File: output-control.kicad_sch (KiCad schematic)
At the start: 57 parts, among them U16 ADS7828, U17 TCA9534PWR, U18 ADS7828

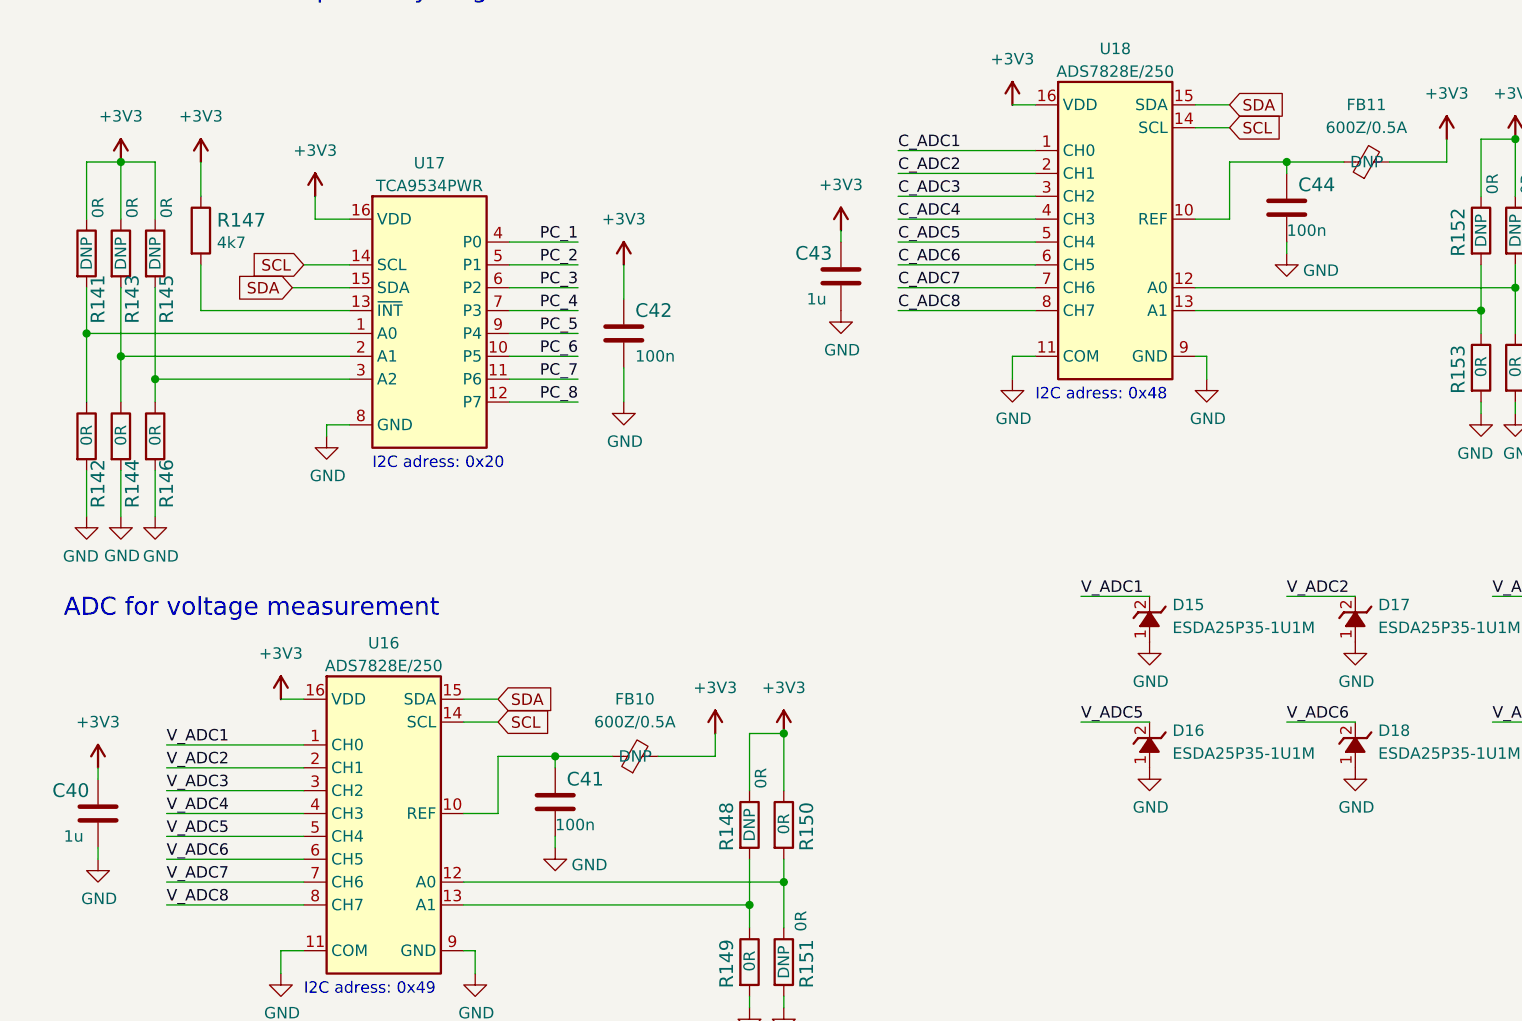
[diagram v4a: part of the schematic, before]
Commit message: Standarize mechanicals and output control
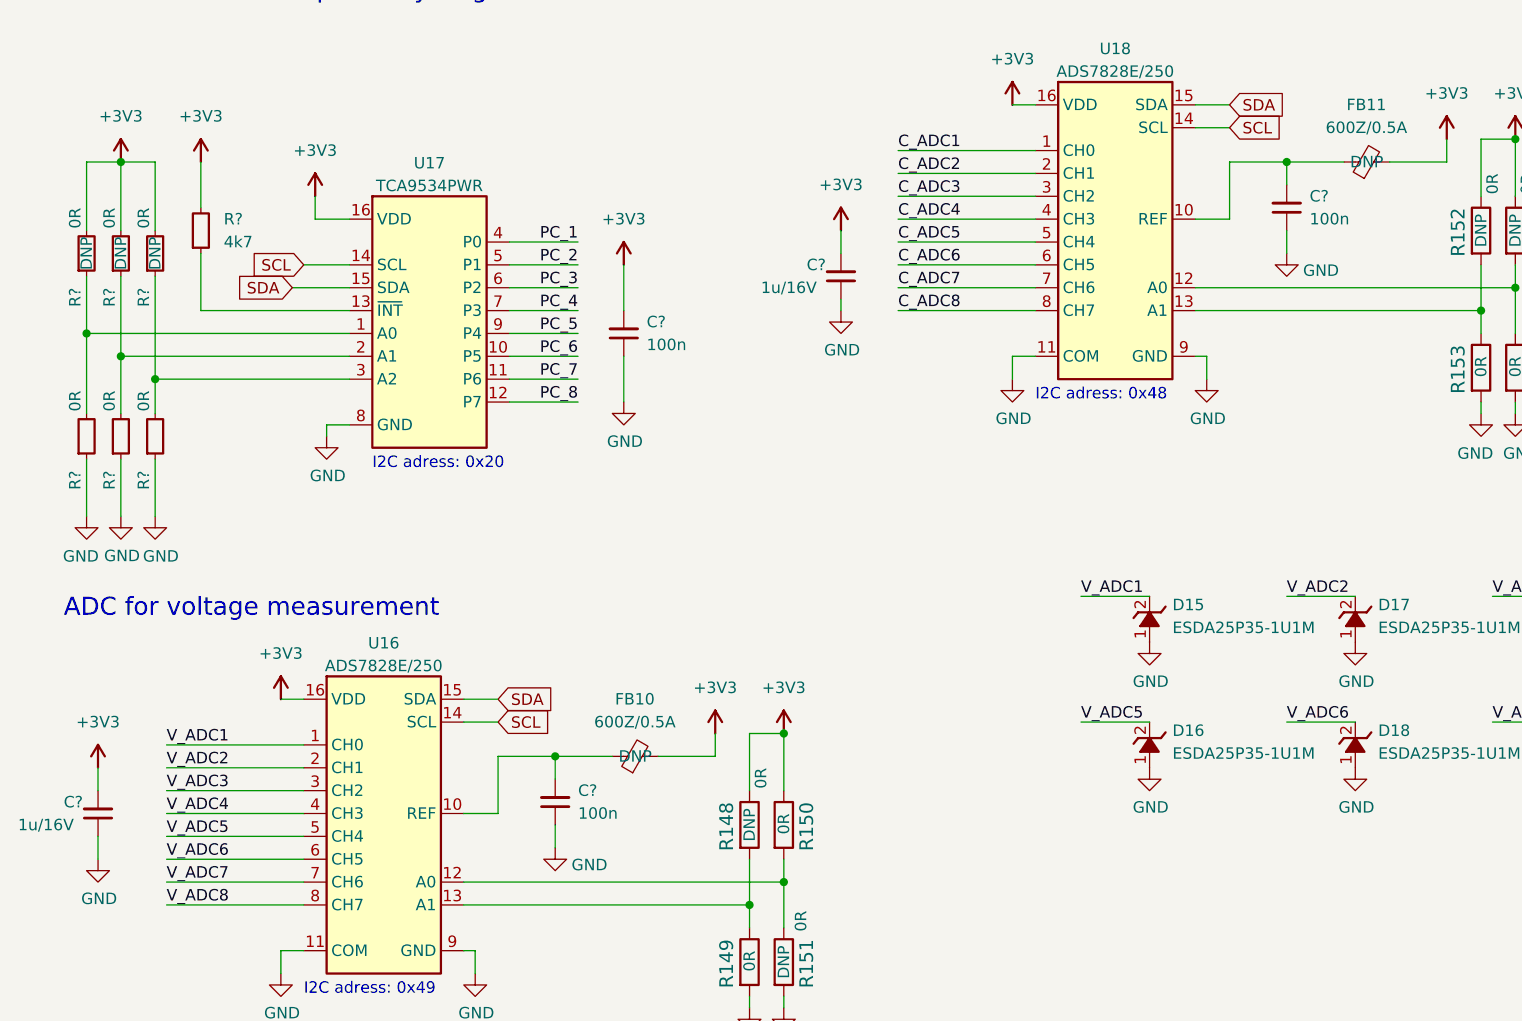
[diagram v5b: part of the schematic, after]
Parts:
- removed C40, C43: C_1u_0402, antmicro-footprints:C_0402_1005Metric, symbol antmicroCapacitors0402:C_1u_0402
- removed C41, C42, C44: C_100n_0402, antmicro-footprints:C_0402_1005Metric, symbol antmicroCapacitors0402:C_100n_0402
- removed R141, R142, R143, R144, R145, R146: R_0R_0402, antmicro-footprints:R_0402_1005Metric, symbol antmicroResistors0402:R_0R_0402
- removed R147: R_4k7_0402, antmicro-footprints:R_0402_1005Metric, symbol antmicroResistors0402:R_4k7_0402
- added C? (x3): C_100n_0402, antmicro-footprints:C_0402_1005Metric, symbol antmicroCapacitors0402:C_100n_0402
- added C? (x2): C_1u_16V_0402, antmicro-footprints:C_0402_1005Metric, symbol antmicroCapacitors0402:C_1u_16V_0402
- added R? (x6): R_0R_0402, antmicro-footprints:R_0402_1005Metric, symbol antmicroResistors0402:R_0R_0402
- added R?: R_4k7_0402, antmicro-footprints:R_0402_1005Metric, symbol antmicroResistors0402:R_4k7_0402
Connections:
- net +3V3: now also C?.2, C?.2, C?.2, R?.2, R?.2, R?.2, R?.2
- net GND: now also C?.1, C?.1, C?.1, C?.1, C?.1, R?.1, R?.1, R?.1
- net at U17.1 (A0): now also R?.1, R?.2
- net at U17.13 (~{INT}): now also R?.1
- net at FB11.1, U18.10 (REF): now also C?.2
- net at U17.2 (A1): now also R?.1, R?.2
- net at FB10.1, U16.10 (REF): now also C?.2
- net at U17.3 (A2): now also R?.1, R?.2

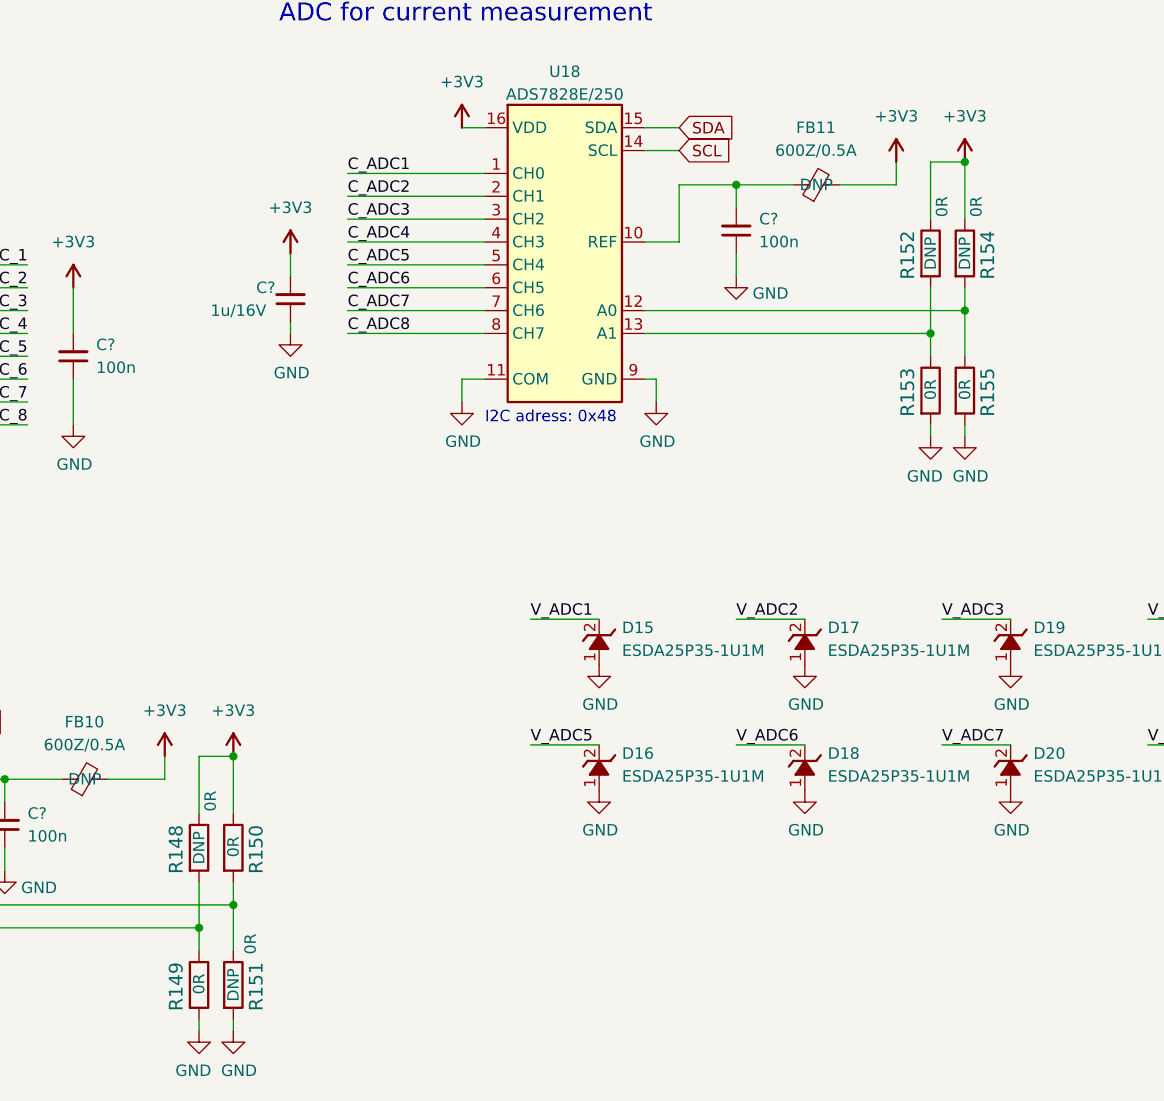
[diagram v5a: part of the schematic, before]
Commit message: Replace outpouts components
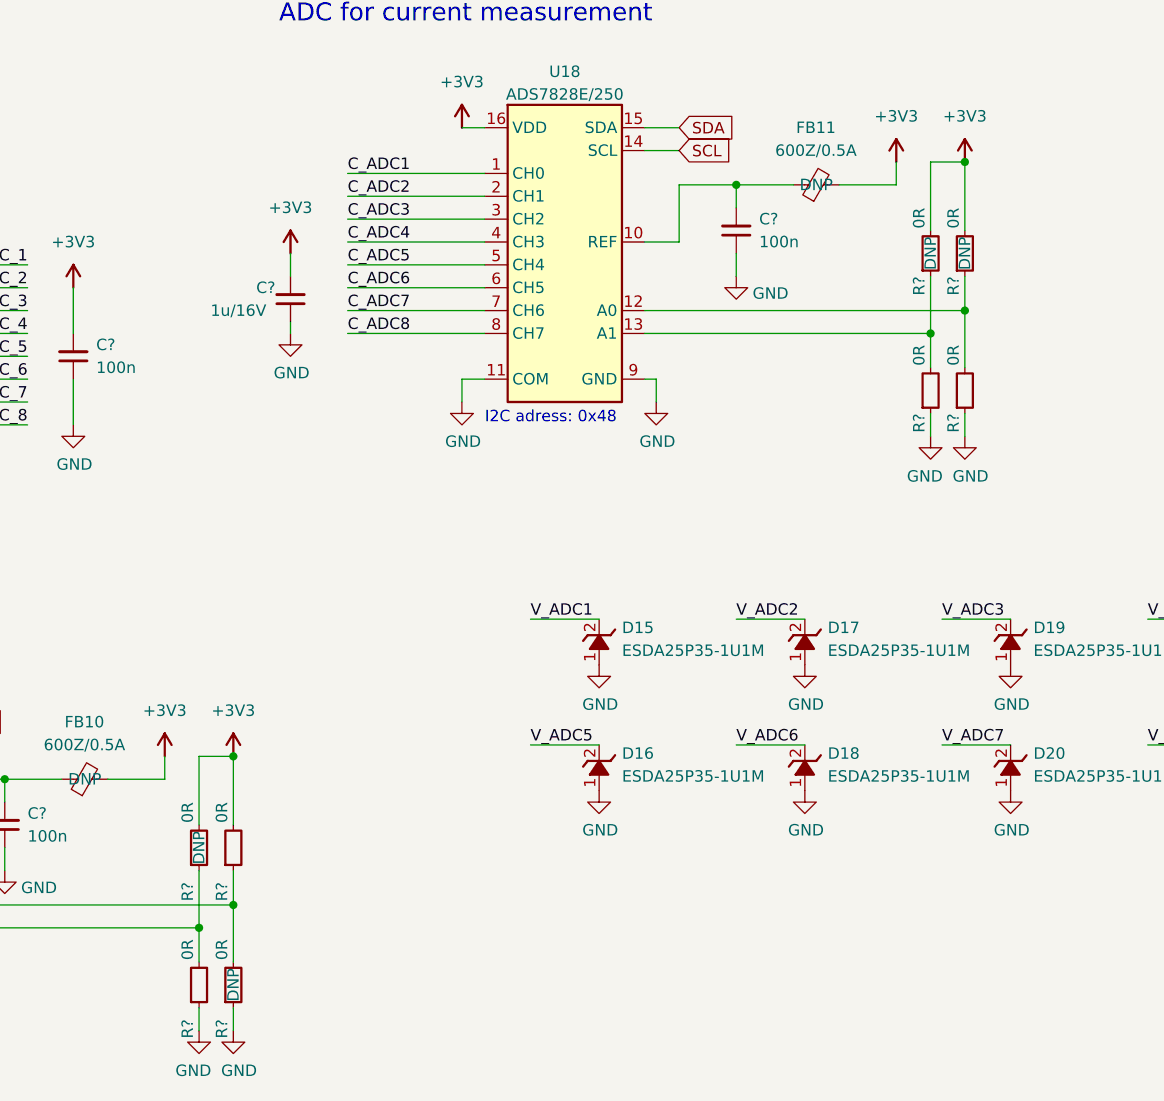
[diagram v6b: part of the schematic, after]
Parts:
- removed R148, R149, R150, R151, R152, R153, R154, R155: R_0R_0402, antmicro-footprints:R_0402_1005Metric, symbol antmicroResistors0402:R_0R_0402
- added R? (x8): R_0R_0402, antmicro-footprints:R_0402_1005Metric, symbol antmicroResistors0402:R_0R_0402
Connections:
- net +3V3: now also R?.2, R?.2, R?.2, R?.2
- net GND: now also R?.1, R?.1, R?.1, R?.1
- net at U16.12 (A0): now also R?.1, R?.2
- net at U18.12 (A0): now also R?.1, R?.2
- net at U18.13 (A1): now also R?.1, R?.2
- net at U16.13 (A1): now also R?.1, R?.2
